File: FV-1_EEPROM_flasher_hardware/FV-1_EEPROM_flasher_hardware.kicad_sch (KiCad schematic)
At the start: 22 parts, among them J1 TFT_SD, J2 SD_Card_Device, J3 Micro_SD_Card_Det2, SW1 Up, SW2 Down, SW3 Right, SW4 Left, SW5 select, U1 24LC32, U2 24LC32

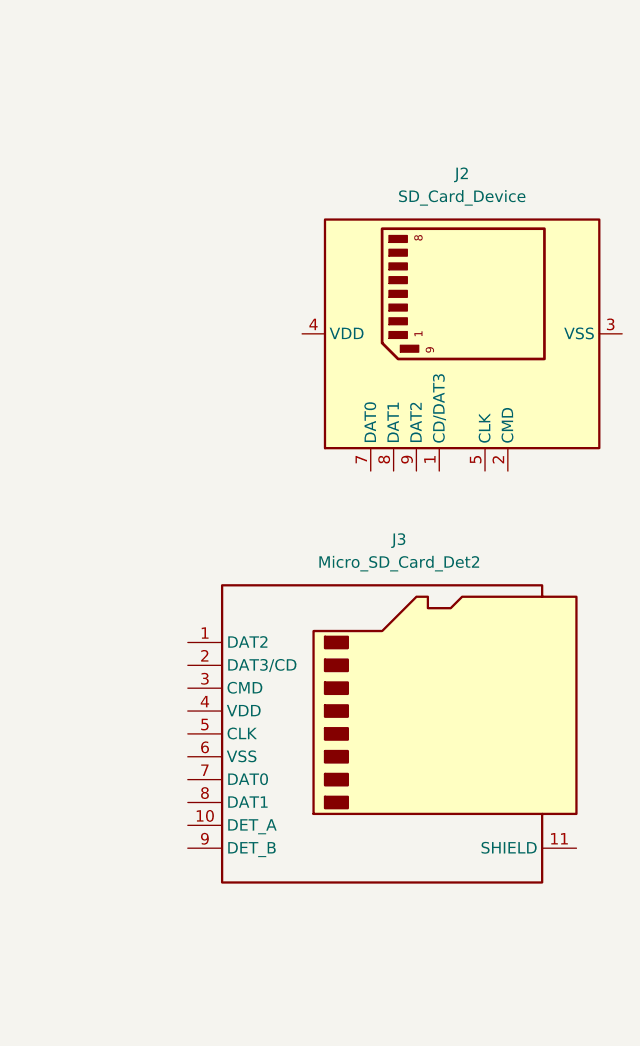
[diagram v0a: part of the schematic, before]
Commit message: removed unused SD card symbols
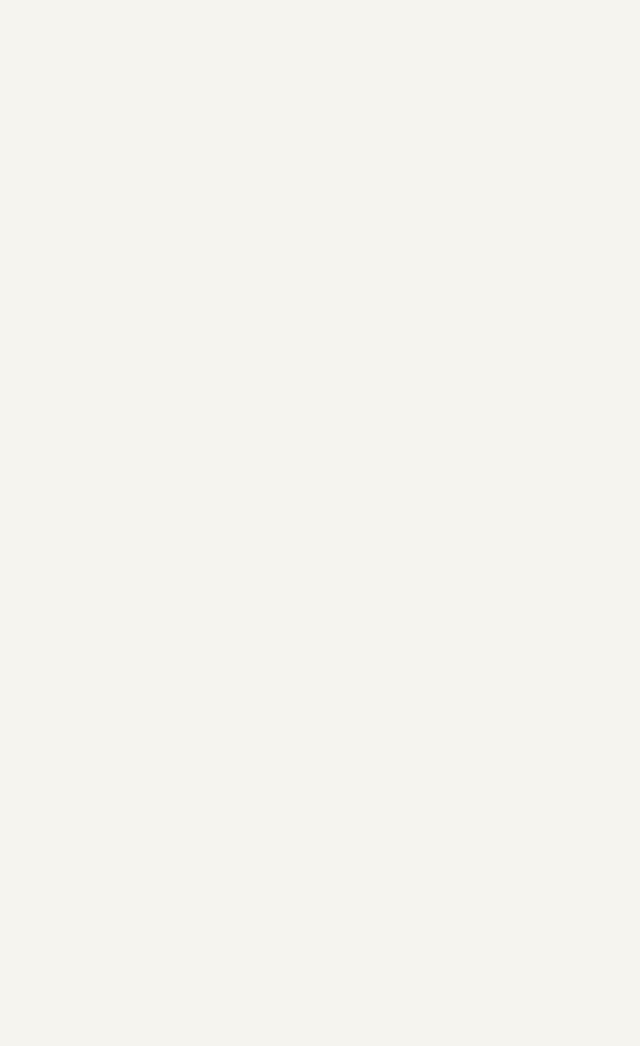
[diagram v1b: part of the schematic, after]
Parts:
- removed J2: SD_Card_Device, symbol Connector:SD_Card_Device
- removed J3: Micro_SD_Card_Det2, symbol Connector:Micro_SD_Card_Det2
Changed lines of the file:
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@@
-	)
-	(symbol
-		(lib_id "Connector:Micro_SD_Card_Det2")
-		(at 247.65 127 0)
-		(unit 1)
-		(exclude_from_sim no)
-		(in_bom yes)
-		(on_board yes)
-		(dnp no)
-		(fields_autoplaced yes)
-		(property "Reference" "J3"
-			(at 248.285 105.41 0)
-			(effects
-				(font
-					(size 1.27 1.27)
-				)
-			)
-		)
-		(property "Value" "Micro_SD_Card_Det2"
-			(at 248.285 107.95 0)
-			(effects
-				(font
-					(size 1.27 1.27)
-				)
-			)
-		)
-		(property "Footprint" ""
-			(at 299.72 109.22 0)
-			(effects
-				(font
-					(size 1.27 1.27)
-				)
-				(hide yes)
-			)
-		)
-		(property "Datasheet" "https://www.hirose.com/en/product/document?clcode=&productname=&series=DM3&documenttype=Catalog&lang=en&documentid=D49662_en"
-			(at 250.19 124.46 0)
-			(effects
-				(font
-					(size 1.27 1.27)
-				)
-				(hide yes)
-			)
-		)
-		(property "Description" "Micro SD Card Socket with two card detection pins"
-			(at 247.65 127 0)
-			(effects
-				(font
-					(size 1.27 1.27)
-				)
-				(hide yes)
-			)
-		)
-		(pin "3"
-		)
-		(pin "2"
-		)
-		(pin "6"
-		)
-		(pin "7"
-		)
-		(pin "11"
-		)
-		(pin "8"
-		)
-		(pin "9"
-		)
-		(pin "1"
-		)
-		(pin "10"
-		)
-		(pin "5"
-		)
-		(pin "4"
-		)
-		(instances
-			(project ""
-				(path "/d848af7e-e260-4acd-aa15-af80787dd2b3"
-					(reference "J3")
-					(unit 1)
-				)
-			)
-		)
 	)
 	(symbol
@@
 					(unit 1)
 				)
-			)
-		)
-	)
-	(symbol
-		(lib_id "Connector:SD_Card_Device")
-		(at 255.27 82.55 90)
-		(unit 1)
-		(exclude_from_sim no)
-		(in_bom yes)
-		(on_board yes)
-		(dnp no)
-		(fields_autoplaced yes)
-		(property "Reference" "J2"
-			(at 255.27 64.77 90)
-			(effects
-				(font
-					(size 1.27 1.27)
-				)
-			)
-		)
-		(property "Value" "SD_Card_Device"
-			(at 255.27 67.31 90)
-			(effects
-				(font
-					(size 1.27 1.27)
-				)
-			)
-		)
-		(property "Footprint" ""
-			(at 255.27 82.55 0)
-			(effects
-				(font
-					(size 1.27 1.27)
-				)
-				(hide yes)
-			)
-		)
-		(property "Datasheet" "http://www.convict.lu/pdf/ProdManualSDCardv1.9.pdf"
-			(at 255.27 82.55 0)
-			(effects
-				(font
-					(size 1.27 1.27)
-				)
-				(hide yes)
-			)
-		)
-		(property "Description" "SD card device/card"
-			(at 255.27 82.55 0)
-			(effects
-				(font
-					(size 1.27 1.27)
-				)
-				(hide yes)
-			)
-		)
-		(pin "5"
-		)
-		(pin "2"
-		)
-		(pin "4"
-		)
-		(pin "6"
-		)
-		(pin "1"
-		)
-		(pin "3"
-		)
-		(pin "9"
-		)
-		(pin "8"
-		)
-		(pin "7"
-		)
-		(instances
-			(project ""
-				(path "/d848af7e-e260-4acd-aa15-af80787dd2b3"
-					(reference "J2")
-					(unit 1)
-				)

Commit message: replaced status led with shift button, led connected to EEPROM write protect pin
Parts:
- added SW6: select, Button_Switch_THT:SW_PUSH_6mm_H5mm, symbol Switch:SW_Push
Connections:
- net EEPROM_WP: now also R3.1
- net GND: now also SW6.2
- net Pgrm_Led renamed btn_shift
- net btn_shift: now also SW6.1; no longer R3.1
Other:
- note added: "shift button uses internal pullup"
- moved on the sheet: D1, R3
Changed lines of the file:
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@@
 		)
 	)
+	(text "shift button\nuses internal\npullup"
+		(exclude_from_sim no)
+		(at 220.98 19.304 0)
+		(effects
+			(font
+				(size 1.27 1.27)
+			)
+		)
+	)
 	(junction
 		(at 163.83 77.47)
@@
 	(wire
 		(pts
-			(xy 67.31 97.79) (xy 54.61 97.79)
-		)
-		(stroke
-			(width 0)
-			(type default)
-		)
-	)
-	(wire
-		(pts
 			(xy 99.06 177.8) (xy 100.33 177.8)
 		)
@@
 	(wire
 		(pts
+			(xy 20.32 99.06) (xy 20.32 97.79)
+		)
+		(stroke
+			(width 0)
+			(type default)
+		)
+	)
+	(wire
+		(pts
 			(xy 100.33 172.72) (xy 99.06 172.72)
 		)
@@
 	(wire
 		(pts
-			(xy 54.61 101.6) (xy 54.61 100.33)
+			(xy 36.83 97.79) (xy 67.31 97.79)
 		)
 		(stroke
@@
 	(wire
 		(pts
+			(xy 194.31 24.13) (xy 203.2 24.13)
+		)
+		(stroke
+			(width 0)
+			(type default)
+		)
+	)
+	(wire
+		(pts
 			(xy 182.88 95.25) (xy 182.88 96.52)
 		)
@@
 	(wire
 		(pts
+			(xy 20.32 97.79) (xy 21.59 97.79)
+		)
+		(stroke
+			(width 0)
+			(type default)
+		)
+	)
+	(wire
+		(pts
 			(xy 163.83 29.21) (xy 165.1 29.21)
 		)
@@
 		)
 	)
-	(label "TFT_SCK"
-		(at 177.8 107.95 180)
+	(label "btn_shift"
+		(at 194.31 24.13 0)
 		(effects
 			(font
 				(size 1.27 1.27)
 			)
-			(justify right bottom)
+			(justify left bottom)
 		)
 	)
-	(label "btn_down"
-		(at 153.67 77.47 0)
+	(label "TFT_SCK"
+		(at 177.8 107.95 180)
 		(effects
 			(font
 				(size 1.27 1.27)
 			)
-			(justify left bottom)
+			(justify right bottom)
 		)
 	)
-	(label "Pgrm_Led"
-		(at 57.15 100.33 0)
+	(label "btn_down"
+		(at 153.67 77.47 0)
 		(effects
 			(font
@@
 		)
 	)
+	(label "btn_shift"
+		(at 54.61 100.33 0)
+		(effects
+			(font
+				(size 1.27 1.27)
+			)
+			(justify left bottom)
+		)
+	)
 	(label "SD_MISO"
 		(at 123.19 64.77 180)
@@
 	(symbol
 		(lib_id "power:GND")
-		(at 54.61 116.84 0)
+		(at 20.32 99.06 0)
 		(unit 1)
 		(exclude_from_sim no)
@@
 		(on_board yes)
 		(dnp no)
-		(fields_autoplaced yes)
 		(property "Reference" "#PWR017"
-			(at 54.61 123.19 0)
+			(at 20.32 105.41 0)
 			(effects
 				(font
@@
 		)
 		(property "Value" "GND"
-			(at 54.61 121.92 0)
+			(at 18.542 103.378 0)
 			(effects
 				(font
 					(size 1.27 1.27)
 				)
+				(justify left)
 			)
 		)
 		(property "Footprint" ""
-			(at 54.61 116.84 0)
+			(at 20.32 99.06 0)
 			(effects
 				(font
@@
 		)
 		(property "Datasheet" ""
-			(at 54.61 116.84 0)
+			(at 20.32 99.06 0)
 			(effects
 				(font
@@
 		)
 		(property "Description" "Power symbol creates a global label with name \"GND\" , ground"
-			(at 54.61 116.84 0)
+			(at 20.32 99.06 0)
 			(effects
 				(font
@@
 	(symbol
 		(lib_id "Device:LED")
-		(at 54.61 113.03 90)
+		(at 25.4 97.79 0)
+		(mirror x)
 		(unit 1)
 		(exclude_from_sim no)
@@
 		(on_board yes)
 		(dnp no)
-		(fields_autoplaced yes)
 		(property "Reference" "D1"
-			(at 58.42 113.3474 90)
+			(at 26.67 92.71 0)
 			(effects
 				(font
@@
 		)
 		(property "Value" "LED"
-			(at 58.42 115.8874 90)
+			(at 27.178 94.742 0)
 			(effects
 				(font
@@
 		)
 		(property "Footprint" "LED_SMD:LED_0805_2012Metric_Pad1.15x1.40mm_HandSolder"
-			(at 54.61 113.03 0)
+			(at 25.4 97.79 0)
 			(effects
 				(font
@@
 		)
 		(property "Datasheet" "~"
-			(at 54.61 113.03 0)
+			(at 25.4 97.79 0)
 			(effects
 				(font
@@
 		)
 		(property "Description" "Light emitting diode"
-			(at 54.61 113.03 0)
+			(at 25.4 97.79 0)
 			(effects
 				(font
@@
 		)
 		(property "Sim.Pins" "1=K 2=A"
-			(at 54.61 113.03 0)
+			(at 25.4 97.79 0)
 			(effects
 				(font
@@
 	)
 	(symbol
+		(lib_id "power:GND")
+		(at 213.36 24.13 0)
+		(unit 1)
+		(exclude_from_sim no)
+		(in_bom yes)
+		(on_board yes)
+		(dnp no)
+		(property "Reference" "#PWR027"
+			(at 213.36 30.48 0)
+			(effects
+				(font
+					(size 1.27 1.27)
+				)
+				(hide yes)
+			)
+		)
+		(property "Value" "GND"
+			(at 213.36 28.194 0)
+			(effects
+				(font
+					(size 1.27 1.27)
+				)
+			)
+		)
+		(property "Footprint" ""
+			(at 213.36 24.13 0)
+			(effects
+				(font
+					(size 1.27 1.27)
+				)
+				(hide yes)
+			)
+		)
+		(property "Datasheet" ""
+			(at 213.36 24.13 0)
+			(effects
+				(font
+					(size 1.27 1.27)
+				)
+				(hide yes)
+			)
+		)
+		(property "Description" "Power symbol creates a global label with name \"GND\" , ground"
+			(at 213.36 24.13 0)
+			(effects
+				(font
+					(size 1.27 1.27)
+				)
+				(hide yes)
+			)
+		)
+		(pin "1"
+		)
+		(instances
+			(project "FV-1_EEPROM_flasher_hardware"
+				(path "/d848af7e-e260-4acd-aa15-af80787dd2b3"
+					(reference "#PWR027")
+					(unit 1)
+				)
+			)
+		)
+	)
+	(symbol
 		(lib_id "power:+3V3")
 		(at 135.89 128.27 0)
@@
 	(symbol
 		(lib_id "Device:R")
-		(at 54.61 105.41 0)
+		(at 33.02 97.79 270)
 		(unit 1)
 		(exclude_from_sim no)
@@
 		(on_board yes)
 		(dnp no)
-		(fields_autoplaced yes)
 		(property "Reference" "R3"
-			(at 57.15 104.1399 0)
+			(at 31.496 92.71 90)
 			(effects
 				(font
@@
 		)
 		(property "Value" "4K7"
-			(at 57.15 106.6799 0)
+			(at 30.988 94.488 90)
 			(effects
 				(font
@@
 		)
 		(property "Footprint" "Resistor_SMD:R_0805_2012Metric_Pad1.20x1.40mm_HandSolder"
-			(at 52.832 105.41 90)
+			(at 33.02 96.012 90)
 			(effects
 				(font
@@
 		)
 		(property "Datasheet" "~"
-			(at 54.61 105.41 0)
+			(at 33.02 97.79 0)
 			(effects
 				(font
@@
 		)
 		(property "Description" "Resistor"
-			(at 54.61 105.41 0)
+			(at 33.02 97.79 0)
 			(effects
 				(font
@@
 					(unit 1)
 				)
+			)
+		)
+	)
+	(symbol
+		(lib_id "Switch:SW_Push")
+		(at 208.28 24.13 0)
+		(unit 1)
+		(exclude_from_sim no)
+		(in_bom yes)
+		(on_board yes)
+		(dnp no)
+		(fields_autoplaced yes)
+		(property "Reference" "SW6"
+			(at 208.28 16.51 0)
+			(effects
+				(font
+					(size 1.27 1.27)
+				)
+			)
+		)
+		(property "Value" "select"
+			(at 208.28 19.05 0)
+			(effects
+				(font
+					(size 1.27 1.27)
+				)
+			)
+		)
+		(property "Footprint" "Button_Switch_THT:SW_PUSH_6mm_H5mm"
+			(at 208.28 19.05 0)
+			(effects
+				(font
+					(size 1.27 1.27)
+				)
+				(hide yes)
+			)
+		)
+		(property "Datasheet" "~"
+			(at 208.28 19.05 0)
+			(effects
+				(font
+					(size 1.27 1.27)
+				)
+				(hide yes)
+			)
+		)
+		(property "Description" "Push button switch, generic, two pins"
+			(at 208.28 24.13 0)
+			(effects
+				(font
+					(size 1.27 1.27)
+				)
+				(hide yes)
+			)
+		)
+		(pin "1"
+		)
+		(pin "2"
+		)
+		(instances
+			(project "FV-1_EEPROM_flasher_hardware"
+				(path "/d848af7e-e260-4acd-aa15-af80787dd2b3"
+					(reference "SW6")
+					(unit 1)
+				)
